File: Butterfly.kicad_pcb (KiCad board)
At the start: 2 copper layers, 93.1 x 65.5 mm, 28 parts, among them J1 Conn_02x03_Odd_Even, J2 USB_A, U1 ATTINY85-20PU

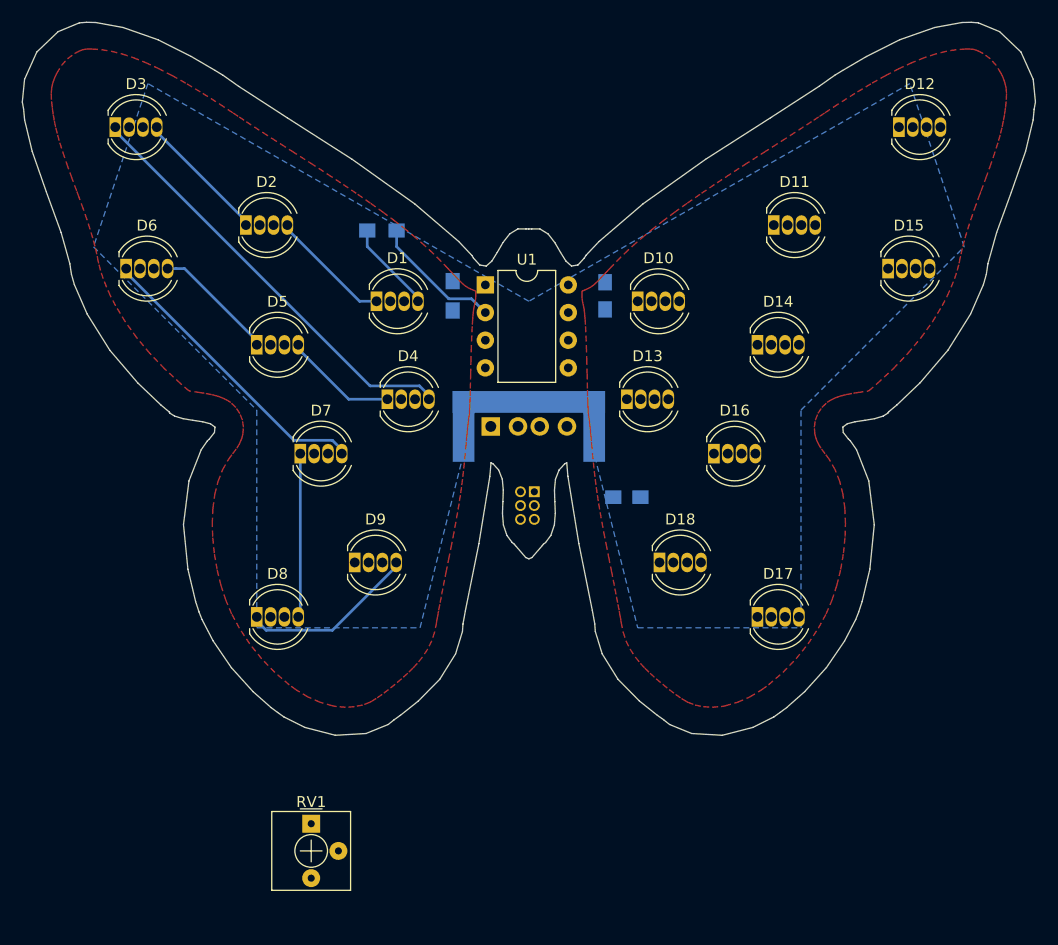
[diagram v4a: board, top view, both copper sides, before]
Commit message: Routing more tracks.
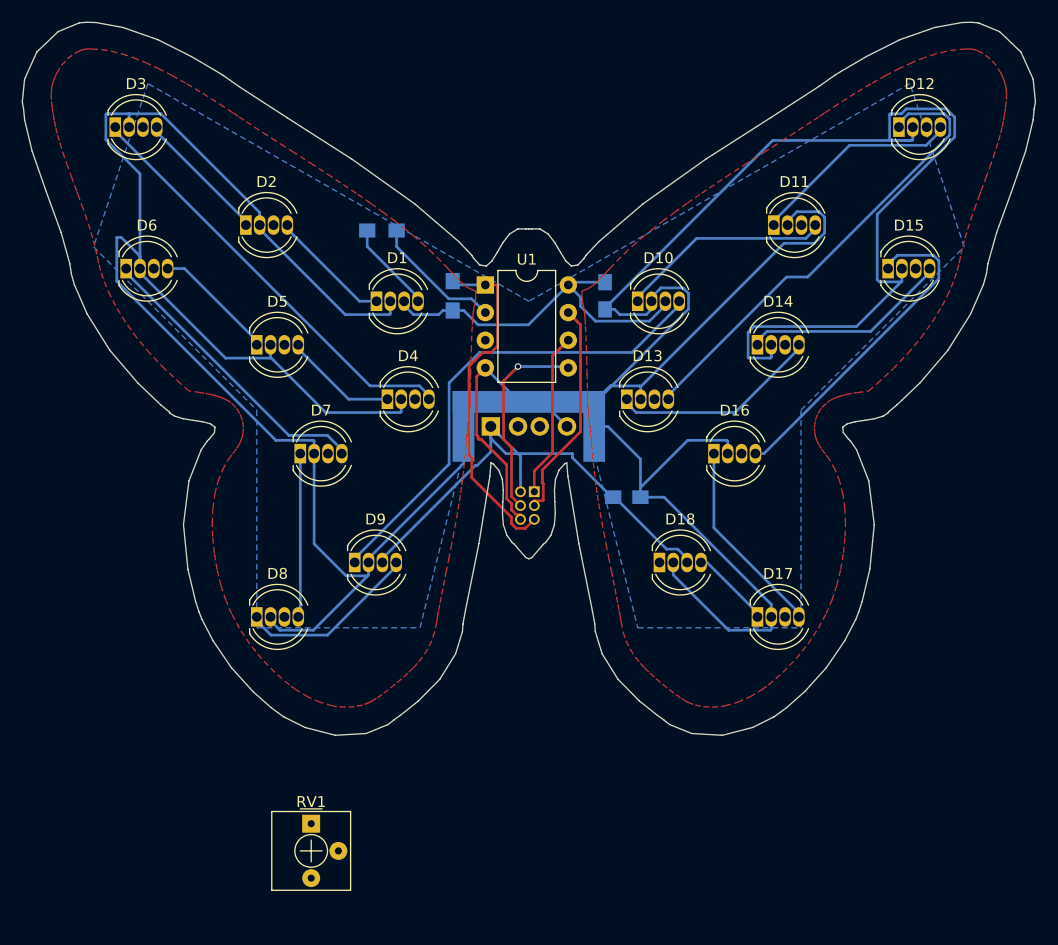
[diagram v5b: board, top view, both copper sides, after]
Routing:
- net GND: track 0.00 -> 391.6 mm
- net +5V: track 0.00 -> 81.4 mm
- net Net-(D10-Pad4): track 0.00 -> 44.6 mm
- net Net-(D12-Pad1): track 0.00 -> 43.2 mm
- net Net-(J1-Pad5): track 0.00 -> 32.0 mm
- net Net-(D15-Pad1): track 0.00 -> 30.8 mm
- net Net-(J1-Pad3): track 0.00 -> 20.5 mm
- net Net-(D10-Pad1): track 0.00 -> 19.6 mm
- net Net-(D11-Pad1): track 0.00 -> 19.5 mm
- net Net-(D13-Pad1): track 0.00 -> 19.3 mm
- net Net-(D14-Pad1): track 0.00 -> 19.1 mm
- net Net-(J1-Pad4): track 0.00 -> 18.6 mm, vias 0 -> 1
- net Net-(D16-Pad1): track 0.00 -> 18.2 mm
- net Net-(J1-Pad1): track 0.00 -> 15.2 mm
- net Net-(D17-Pad1): track 0.00 -> 7.47 mm

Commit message: I think I got everything to fit.
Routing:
- net GND: track 391.6 -> 401.3 mm
- net Net-(J1-Pad5): track 32.0 -> 34.4 mm

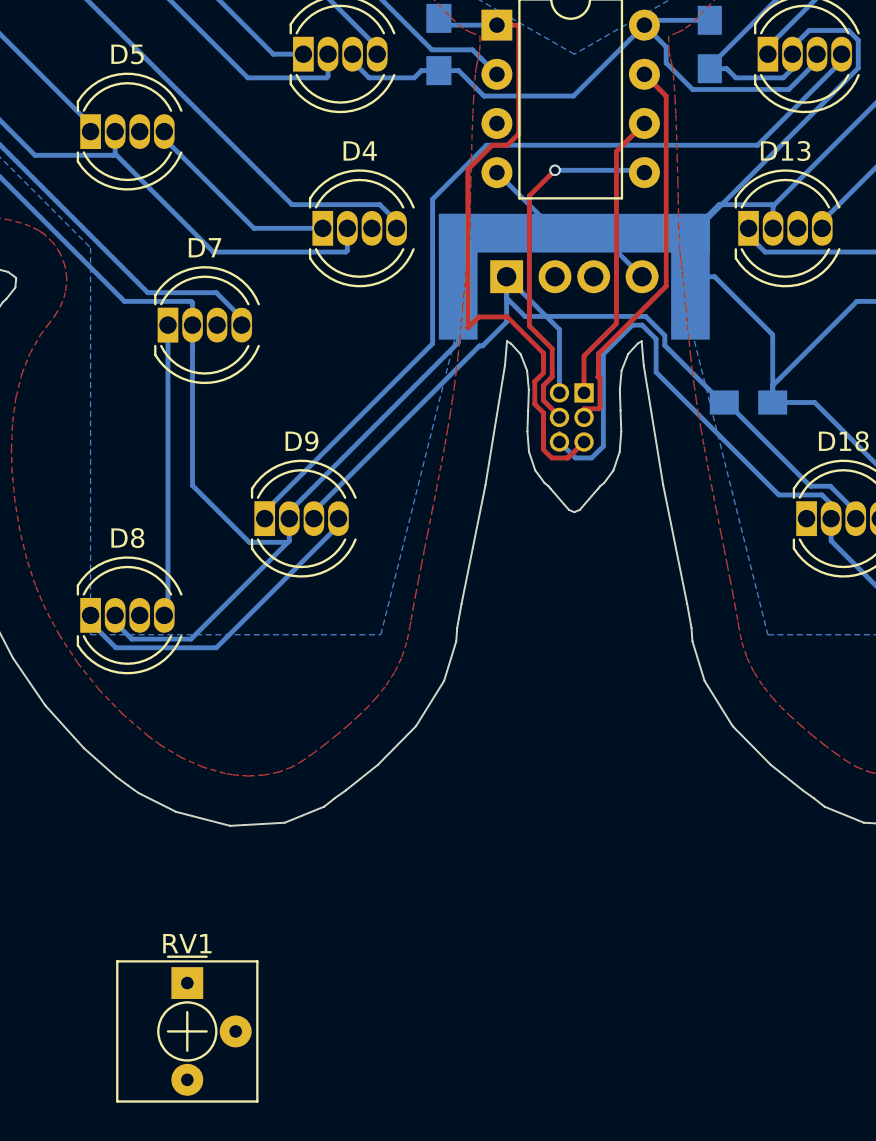
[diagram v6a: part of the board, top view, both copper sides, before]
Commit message: Place potentiometer.
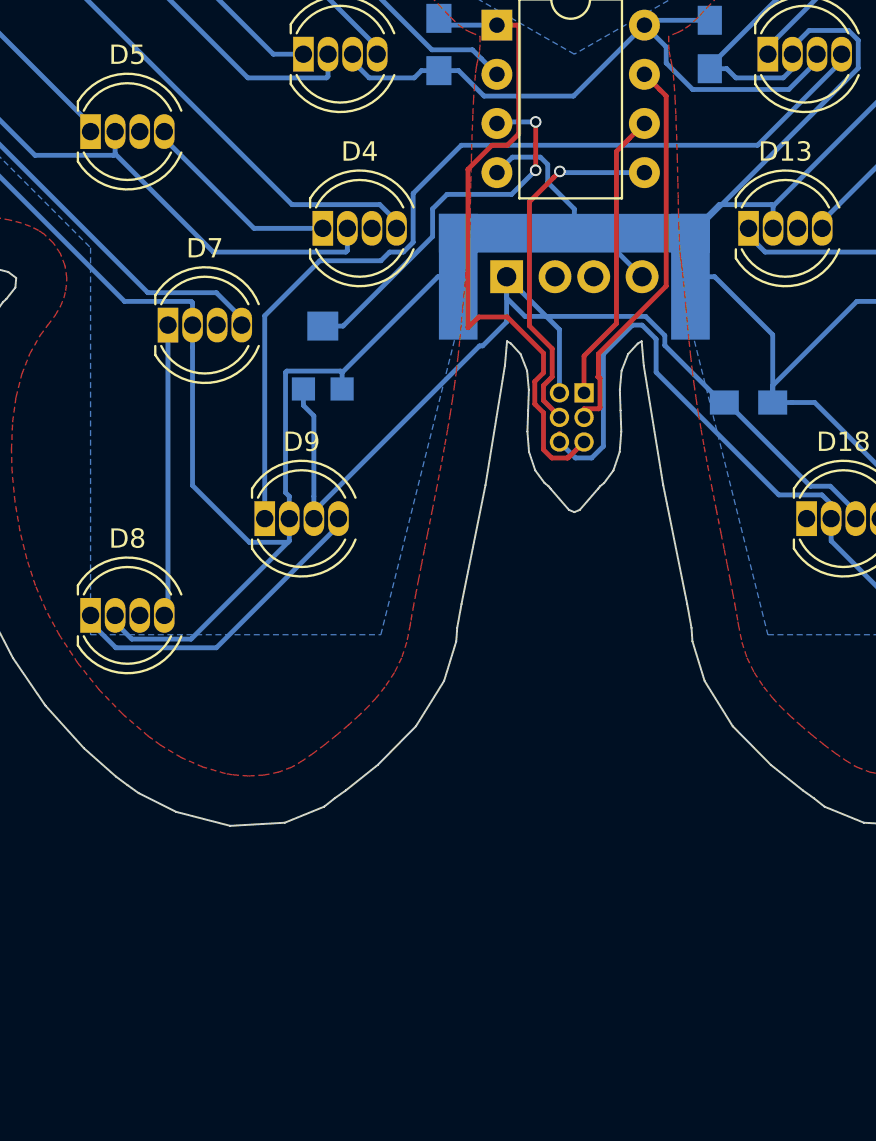
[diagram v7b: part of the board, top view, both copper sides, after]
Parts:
- removed RV1: 10k, Potentiometers:Potentiometer_Trimmer_Copal_CT-6EP
- added POT1: TC33X-2-103E, digikey-footprints:TC33X-2-103E, B.Cu at (132.0, 110.5)
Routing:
- net Net-(POT1-Pad2): track 0.00 -> 19.7 mm, vias 0 -> 2
- net +5V: track 81.5 -> 88.4 mm
- net GND: track 401.3 -> 407.0 mm
- net Net-(D10-Pad4): track 44.6 -> 47.6 mm

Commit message: Set design rules.
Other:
- net class Default: clearance 0.2 -> 0.1524; trace_width 0.25 -> 0.1524
- rule trace_clearance: 0.2 -> 0.1524
- rule trace_min: 0.2 -> 0.1524
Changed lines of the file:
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@@
   )
   (setup
-    (last_trace_width 0.25)
-    (trace_clearance 0.2)
+    (last_trace_width 0.1524)
+    (trace_clearance 0.1524)
     (zone_clearance 0.508)
     (zone_45_only no)
-    (trace_min 0.2)
+    (trace_min 0.1524)
     (segment_width 0.2)
     (edge_width 0.15)
@@
   (net 29 "Net-(POT1-Pad2)")
   (net_class Default "This is the default net class."
-    (clearance 0.2)
-    (trace_width 0.25)
+    (clearance 0.1524)
+    (trace_width 0.1524)
     (via_dia 0.6)
     (via_drill 0.4)
